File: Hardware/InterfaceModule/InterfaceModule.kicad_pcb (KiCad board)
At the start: 2 copper layers, 25 parts, among them J1 External MIC IN, J11 D-700 GPS, J12 D-700 COM, J13 D-700 MIC, J2 External COM, J3 GPS IN, J4 External GPS IN, J5 TS-480 MIC, J7 TS-480 COM, J8 TS-480 EXT.SP, J9 D-700 EXT.SP 1, K1 4PDT Relay, K10 3PDT Relay, K11 3PDT Relay, K12 3PDT Relay, K13 3PDT Relay, K14 3PDT Relay, K2 4PDT Relay, K3 4PDT Relay, K4 4PDT Relay, K5 3PDT Relay, K6 3PDT Relay, K7 3PDT Relay, K8 3PDT Relay, K9 3PDT Relay

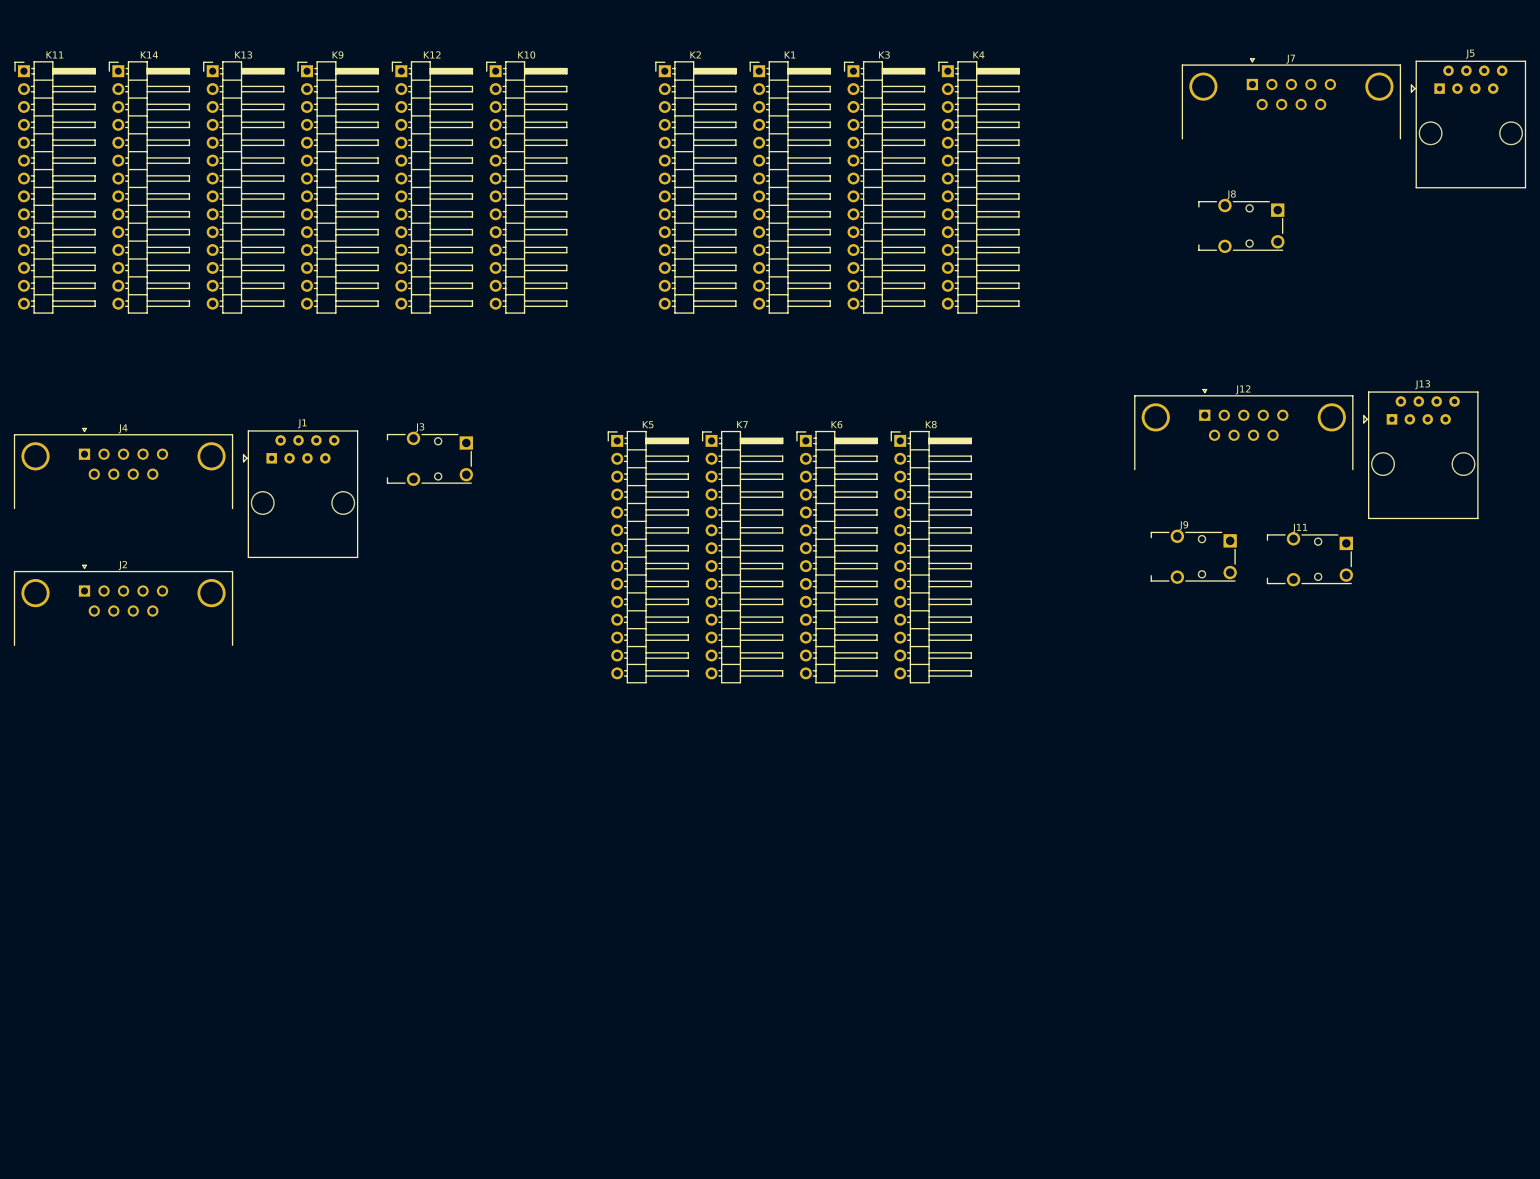
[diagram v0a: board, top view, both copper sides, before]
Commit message: Fixed labels
I don't know how to do busses properly, oh well
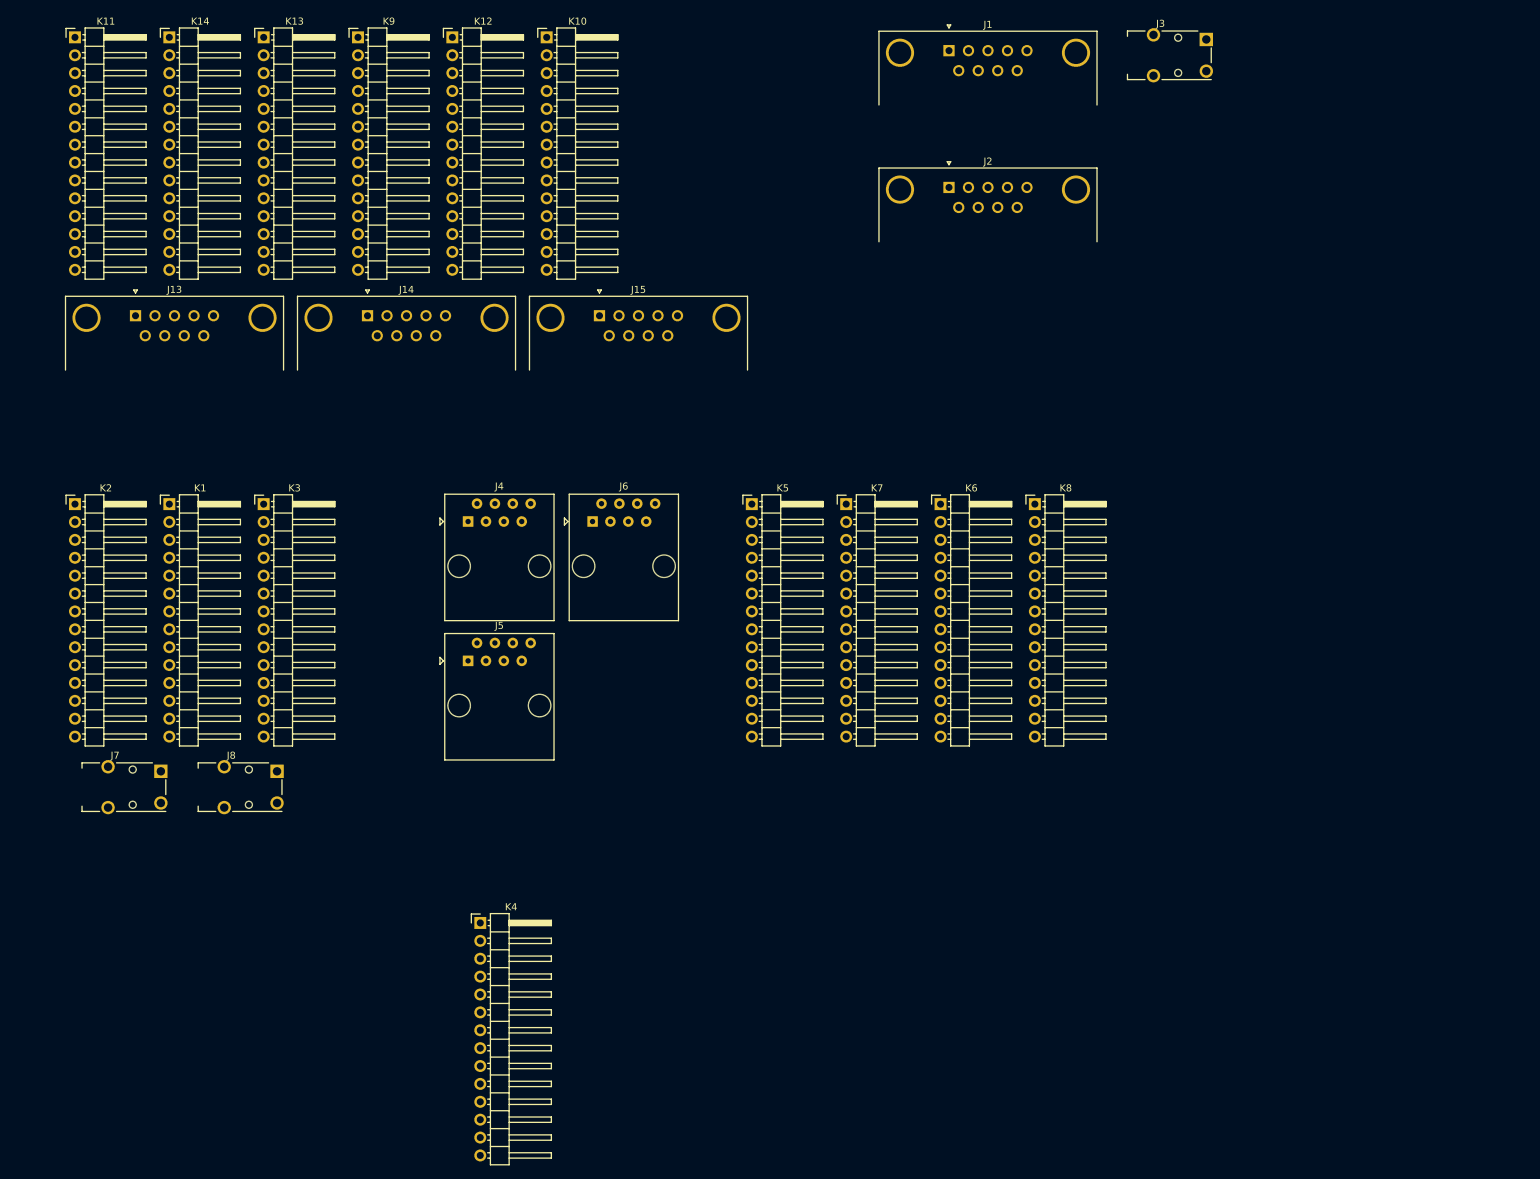
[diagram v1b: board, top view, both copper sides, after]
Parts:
- removed J11: D-700 GPS, Connector_Audio:Jack_3.5mm_Switronic_ST-005-G_horizontal
- removed J12: D-700 COM, Connector_Dsub:DSUB-9_Male_Horizontal_P2.77x2.84mm_EdgePinOffset4.94mm_Housed_MountingHolesOffset7.48mm
- removed J9: D-700 EXT.SP 1, Connector_Audio:Jack_3.5mm_Switronic_ST-005-G_horizontal
- added J14: TS-480 COM, Connector_Dsub:DSUB-9_Male_Horizontal_P2.77x2.84mm_EdgePinOffset4.94mm_Housed_MountingHolesOffset7.48mm, F.Cu at (100.4, 88.5)
- added J15: External COM, Connector_Dsub:DSUB-9_Male_Horizontal_P2.77x2.84mm_EdgePinOffset4.94mm_Housed_MountingHolesOffset7.48mm, F.Cu at (133.4, 88.5)
- added J6: TS-480 MIC, Connector_RJ:RJ45_Amphenol_54602-x08_Horizontal, F.Cu at (132.4, 117.8)
- J1: value External MIC IN -> External GPS IN; footprint Connector_RJ:RJ45_Amphenol_54602-x08_Horizontal -> Connector_Dsub:DSUB-9_Male_Horizontal_P2.77x2.84mm_EdgePinOffset4.94mm_Housed_MountingHolesOffset7.48mm
- J13: value D-700 MIC -> TS-480 COM; footprint Connector_RJ:RJ45_Amphenol_54602-x08_Horizontal -> Connector_Dsub:DSUB-9_Male_Horizontal_P2.77x2.84mm_EdgePinOffset4.94mm_Housed_MountingHolesOffset7.48mm
- J2: value External COM -> External GPS OUT
- J3: value GPS IN -> D-700 GPS
- J4: value External GPS IN -> External MIC IN; footprint Connector_Dsub:DSUB-9_Male_Horizontal_P2.77x2.84mm_EdgePinOffset4.94mm_Housed_MountingHolesOffset7.48mm -> Connector_RJ:RJ45_Amphenol_54602-x08_Horizontal
- J5: value TS-480 MIC -> D-700 MIC
- J7: value TS-480 COM -> D-700 EXT.SP 1; footprint Connector_Dsub:DSUB-9_Male_Horizontal_P2.77x2.84mm_EdgePinOffset4.94mm_Housed_MountingHolesOffset7.48mm -> Connector_Audio:Jack_3.5mm_Switronic_ST-005-G_horizontal
- moved J7 189.9 mm to (64.6, 155.5)
- moved J13 179.1 mm to (67.5, 88.5)
- moved J8 163.0 mm to (81.1, 155.5)
- moved J5 160.1 mm to (114.7, 137.6)
- moved K4 138.0 mm to (116.4, 174.8)
- moved J2 135.5 mm to (183.0, 70.3)
- moved J3 119.7 mm to (213.1, 51.6)
- moved J1 112.3 mm to (183.0, 50.9)
- moved K3 103.9 mm to (85.7, 115.3)
- moved K1 103.9 mm to (72.3, 115.3)
- moved K2 103.9 mm to (58.9, 115.3)
- moved J4 55.3 mm to (114.7, 117.8)
- moved K5 21.1 mm to (155.0, 115.3)
- moved K6 21.1 mm to (181.8, 115.3)
- moved K7 21.1 mm to (168.4, 115.3)
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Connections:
- net /Kenwood D-700 Connectors/D-700_DATA.DATA_DE renamed /Data Port Switching/DATA_DE
- net /Kenwood D-700 Connectors/D-700_DATA.DATA_PKD renamed /Data Port Switching/DATA_PKD
- net /Kenwood D-700 Connectors/D-700_DATA.DATA_PKS renamed /Data Port Switching/DATA_PKS
- net /Kenwood D-700 Connectors/D-700_DATA.DATA_PR1 renamed /Data Port Switching/DATA_PR1
- net /Kenwood D-700 Connectors/D-700_DATA.DATA_PR9 renamed /Data Port Switching/DATA_PR9
- net /Kenwood TS-480 Connectors/TS-480_DATA.DATA_ANG renamed /Data Port Switching/DATA_ANG
- net /Kenwood TS-480 Connectors/TS-480_DATA.DATA_ANI renamed /Data Port Switching/DATA_ANI
- net /Kenwood TS-480 Connectors/TS-480_DATA.DATA_ANO renamed /Data Port Switching/DATA_ANO
- net /Kenwood TS-480 Connectors/TS-480_DATA.DATA_DTS renamed /Data Port Switching/DATA_DTS
- net /Kenwood TS-480 Connectors/TS-480_DATA.DATA_NC renamed /Data Port Switching/DATA_NC
- J1 pad 1: /MIC_UP -> unconnected-(J1-Pad1)
- J1 pad 2: /MIC_8V -> Net-(J1-Pad2)
- J1 pad 3: /MIC_GND -> Net-(J1-Pad3)
- J1 pad 4: /MIC_PTT -> unconnected-(J1-Pad4)
- J1 pad 5: /MIC_MICGND -> GND
- J1 pad 6: /MIC_MIC -> unconnected-(J1-Pad6)
- J1 pad 7: /MIC_NC -> unconnected-(J1-Pad7)
- J1 pad 8: /MIC_DWN -> unconnected-(J1-Pad8)
- J13 pad 1: /Kenwood D-700 Connectors/MIC_UP -> /COM Port Switching/NC1
- J13 pad 2: /Kenwood D-700 Connectors/MIC_8V -> /COM Port Switching/RX
- J13 pad 3: /Kenwood D-700 Connectors/MIC_GND -> /COM Port Switching/TX
- J13 pad 4: /Kenwood D-700 Connectors/MIC_PTT -> /COM Port Switching/DTR
- J13 pad 5: /Kenwood D-700 Connectors/MIC_MICGND -> GND
- J13 pad 6: /Kenwood D-700 Connectors/MIC_MIC -> /COM Port Switching/DSR
- J13 pad 7: /Kenwood D-700 Connectors/MIC_NC -> /COM Port Switching/RTS
- J13 pad 8: /Kenwood D-700 Connectors/MIC_DWN -> /COM Port Switching/CTS
- J2 pad 1: /COM_NC1 -> unconnected-(J2-Pad1)
- J2 pad 2: /COM_RX -> Net-(J1-Pad2)
- J2 pad 3: /COM_TX -> Net-(J1-Pad3)
- J2 pad 4: /COM_DTR -> unconnected-(J2-Pad4)
- J2 pad 5: /COM_GND -> GND
- J2 pad 6: /COM_DSR -> unconnected-(J2-Pad6)
- J2 pad 7: /COM_RTS -> unconnected-(J2-Pad7)
- J2 pad 8: /COM_CTS -> unconnected-(J2-Pad8)
- J2 pad 9: /COM_NC2 -> unconnected-(J2-Pad9)
- J3 pad R: /EXTERNAL_GPS_IN.GPS_IN -> unconnected-(J3-PadR)
- J3 pad T: /EXTERNAL_GPS_IN.GPS_OUT -> Net-(J1-Pad2)
- J4 pad 1: unconnected-(J4-Pad1) -> /Microphone Switching/UP
- J4 pad 2: /EXTERNAL_GPS_IN.GPS_IN -> /Microphone Switching/8V
- J4 pad 3: /EXTERNAL_GPS_IN.GPS_OUT -> GND
- J4 pad 4: unconnected-(J4-Pad4) -> /Microphone Switching/PTT
- J4 pad 5: GND -> /Microphone Switching/MICGND
- J4 pad 6: unconnected-(J4-Pad6) -> /Microphone Switching/MIC
- J4 pad 7: unconnected-(J4-Pad7) -> /Microphone Switching/NC
- J4 pad 8: unconnected-(J4-Pad8) -> /Microphone Switching/DWN
- J5 pad 1: /Kenwood TS-480 Connectors/MIC_UP -> /Microphone Switching/UP
- J5 pad 2: /Kenwood TS-480 Connectors/MIC_8V -> /Microphone Switching/8V
- J5 pad 3: /Kenwood TS-480 Connectors/MIC_GND -> GND
- J5 pad 4: /Kenwood TS-480 Connectors/MIC_PTT -> /Microphone Switching/PTT
- J5 pad 5: /Kenwood TS-480 Connectors/MIC_MICGND -> /Microphone Switching/MICGND
- J5 pad 6: /Kenwood TS-480 Connectors/MIC_MIC -> /Microphone Switching/MIC
- J5 pad 7: /Kenwood TS-480 Connectors/MIC_NC -> /Microphone Switching/NC
- J5 pad 8: /Kenwood TS-480 Connectors/MIC_DWN -> /Microphone Switching/DWN
- J8 pad S: /Kenwood TS-480 Connectors/EXT.SP_S -> /Microphone Switching/SP_S
- J8 pad T: /Kenwood TS-480 Connectors/EXT.SP_T -> /Microphone Switching/SP_T
- K1 pad 11: /Kenwood D-700 Connectors/D-700_MIC.MIC_UP -> /Microphone Switching/UP
- K1 pad 12: /Kenwood D-700 Connectors/D-700_MIC.MIC_8V -> /Microphone Switching/8V
- K1 pad 13: /Kenwood D-700 Connectors/D-700_MIC.MIC_GND -> GND
- K1 pad 14: /Kenwood D-700 Connectors/D-700_MIC.MIC_PTT -> /Microphone Switching/PTT
- K1 pad 2: /Switching Network/Microphone Switching/MICROPHONE.MIC_UP -> /Microphone Switching/UP
- K1 pad 4: /Switching Network/Microphone Switching/MICROPHONE.MIC_8V -> /Microphone Switching/8V
- K1 pad 6: /Switching Network/Microphone Switching/MICROPHONE.MIC_GND -> GND
- K1 pad 8: /Switching Network/Microphone Switching/MICROPHONE.MIC_PTT -> /Microphone Switching/PTT
- K10 pad 2: /Kenwood D-700 Connectors/D-700_COM.COM_DTR -> /COM Port Switching/DTR
- K10 pad 3: /EXTERNAL_COM.COM_DSR -> /COM Port Switching/DSR
- K10 pad 4: /Kenwood D-700 Connectors/D-700_COM.COM_DSR -> /COM Port Switching/DSR
- K10 pad 5: /EXTERNAL_COM.COM_DTR -> /COM Port Switching/DTR
- K10 pad 6: /Kenwood D-700 Connectors/D-700_COM.COM_RX -> /COM Port Switching/RX
- K10 pad 7: /EXTERNAL_COM.COM_TX -> /COM Port Switching/TX
- K11 pad 2: /Kenwood TS-480 Connectors/TS-480_COM.COM_CTS -> /COM Port Switching/CTS
- K11 pad 3: /EXTERNAL_COM.COM_RTS -> /COM Port Switching/RTS
- K11 pad 4: /Kenwood TS-480 Connectors/TS-480_COM.COM_RX -> /COM Port Switching/RX
- K11 pad 5: /EXTERNAL_COM.COM_TX -> /COM Port Switching/TX
- K11 pad 6: /Kenwood TS-480 Connectors/TS-480_COM.COM_RTS -> /COM Port Switching/RTS
- K11 pad 7: /EXTERNAL_COM.COM_CTS -> /COM Port Switching/CTS
- K12 pad 2: /Kenwood D-700 Connectors/D-700_COM.COM_RTS -> /COM Port Switching/RTS
- K12 pad 3: /EXTERNAL_COM.COM_CTS -> /COM Port Switching/CTS
- K12 pad 4: /Kenwood D-700 Connectors/D-700_COM.COM_TX -> /COM Port Switching/TX
- K12 pad 5: /EXTERNAL_COM.COM_RX -> /COM Port Switching/RX
- K12 pad 6: /Kenwood D-700 Connectors/D-700_COM.COM_CTS -> /COM Port Switching/CTS
- K12 pad 7: /EXTERNAL_COM.COM_RTS -> /COM Port Switching/RTS
- K13 pad 2: /Kenwood TS-480 Connectors/TS-480_COM.COM_NC1 -> /COM Port Switching/NC1
- K13 pad 3: /EXTERNAL_COM.COM_NC1 -> /COM Port Switching/NC1
- K13 pad 4: /Kenwood TS-480 Connectors/TS-480_COM.COM_NC2 -> /COM Port Switching/NC2
- K13 pad 5: /EXTERNAL_COM.COM_NC2 -> /COM Port Switching/NC2
- K13 pad 6: /Kenwood TS-480 Connectors/TS-480_COM.COM_GND -> GND
- K13 pad 7: /EXTERNAL_COM.COM_GND -> GND
- K14 pad 2: /Kenwood D-700 Connectors/D-700_COM.COM_NC1 -> /COM Port Switching/NC1
- K14 pad 3: /EXTERNAL_COM.COM_NC1 -> /COM Port Switching/NC1
- K14 pad 4: /Kenwood D-700 Connectors/D-700_COM.COM_NC2 -> /COM Port Switching/NC2
- K14 pad 5: /EXTERNAL_COM.COM_NC2 -> /COM Port Switching/NC2
- K14 pad 6: /Kenwood D-700 Connectors/D-700_COM.COM_GND -> GND
- K14 pad 7: /EXTERNAL_COM.COM_GND -> GND
- K2 pad 11: /Kenwood TS-480 Connectors/TS-480_MIC.MIC_PTT -> /Microphone Switching/PTT
- K2 pad 12: /Kenwood TS-480 Connectors/TS-480_MIC.MIC_GND -> GND
- K2 pad 13: /Kenwood TS-480 Connectors/TS-480_MIC.MIC_8V -> /Microphone Switching/8V
- K2 pad 14: /Kenwood TS-480 Connectors/TS-480_MIC.MIC_UP -> /Microphone Switching/UP
- K2 pad 3: /Switching Network/Microphone Switching/MICROPHONE.MIC_PTT -> /Microphone Switching/PTT
- K2 pad 5: /Switching Network/Microphone Switching/MICROPHONE.MIC_GND -> GND
- K2 pad 7: /Switching Network/Microphone Switching/MICROPHONE.MIC_8V -> /Microphone Switching/8V
- K2 pad 9: /Switching Network/Microphone Switching/MICROPHONE.MIC_UP -> /Microphone Switching/UP
- K3 pad 11: /Switching Network/Microphone Switching/D-700_MIC.MICGND -> /Microphone Switching/MICGND
- K3 pad 12: /Kenwood D-700 Connectors/D-700_MIC.MIC_MIC -> /Microphone Switching/MIC
- K3 pad 13: /Kenwood D-700 Connectors/D-700_MIC.MIC_NC -> /Microphone Switching/NC
- K3 pad 14: /Kenwood D-700 Connectors/D-700_MIC.MIC_DWN -> /Microphone Switching/DWN
- K3 pad 2: /Switching Network/Microphone Switching/MICROPHONE.MIC_MICGND -> /Microphone Switching/MICGND
- K3 pad 3: /Switching Network/Microphone Switching/D-700_EXTSP1.SP_T -> /Microphone Switching/SP_T
- K3 pad 4: /Switching Network/Microphone Switching/MICROPHONE.MIC_MIC -> /Microphone Switching/MIC
- K3 pad 6: /Switching Network/Microphone Switching/MICROPHONE.MIC_NC -> /Microphone Switching/NC
- K3 pad 8: /Switching Network/Microphone Switching/MICROPHONE.MIC_DWN -> /Microphone Switching/DWN
- K4 pad 11: /Kenwood TS-480 Connectors/TS-480_MIC.MIC_DWN -> /Microphone Switching/DWN
- K4 pad 12: /Kenwood TS-480 Connectors/TS-480_MIC.MIC_NC -> /Microphone Switching/NC
- K4 pad 13: /Kenwood TS-480 Connectors/TS-480_MIC.MIC_MIC -> /Microphone Switching/MIC
- K4 pad 14: /Switching Network/Microphone Switching/TS-480_MIC.MICGND -> /Microphone Switching/MICGND
- K4 pad 3: /Switching Network/Microphone Switching/MICROPHONE.MIC_DWN -> /Microphone Switching/DWN
- K4 pad 5: /Switching Network/Microphone Switching/MICROPHONE.MIC_NC -> /Microphone Switching/NC
- K4 pad 7: /Switching Network/Microphone Switching/MICROPHONE.MIC_MIC -> /Microphone Switching/MIC
- K4 pad 8: /Switching Network/Microphone Switching/D-700_EXTSP1.SP_T -> /Microphone Switching/SP_T
- K4 pad 9: /Switching Network/Microphone Switching/MICROPHONE.MIC_MICGND -> /Microphone Switching/MICGND
- K5 pad 3: /SignaLink #2 Connectors/SignaLink4 -> /Data Port Switching/RADIO_4
- K5 pad 5: /SignaLink #2 Connectors/SignaLink1 -> /Data Port Switching/RADIO_1
- K5 pad 7: /SignaLink #2 Connectors/SignaLink5 -> /Data Port Switching/RADIO_5
- K6 pad 3: /SignaLink #1 Connectors/SignaLink0 -> /Data Port Switching/RADIO_0
- K6 pad 5: /SignaLink #1 Connectors/SignaLink1 -> /Data Port Switching/RADIO_1
- K6 pad 6: /Kenwood D-700 Connectors/D-700_DATA.DATA_SQC -> /Data Port Switching/DATA_SQC
- K6 pad 7: /SignaLink #1 Connectors/SignaLink2 -> /Data Port Switching/RADIO_2
- K7 pad 3: /SignaLink #2 Connectors/SignaLink3 -> /Data Port Switching/RADIO_3
- K7 pad 5: /SignaLink #2 Connectors/SignaLink0 -> /Data Port Switching/RADIO_0
- K7 pad 6: /Kenwood TS-480 Connectors/TS-480_DATA.DATA_SQC -> /Data Port Switching/DATA_SQC
- K7 pad 7: /SignaLink #2 Connectors/SignaLink2 -> /Data Port Switching/RADIO_2
- K8 pad 3: /SignaLink #1 Connectors/SignaLink3 -> /Data Port Switching/RADIO_3
- K8 pad 5: /SignaLink #1 Connectors/SignaLink4 -> /Data Port Switching/RADIO_4
- K8 pad 7: /SignaLink #1 Connectors/SignaLink5 -> /Data Port Switching/RADIO_5
- K9 pad 2: /Kenwood TS-480 Connectors/TS-480_COM.COM_DSR -> /COM Port Switching/DSR
- K9 pad 3: /EXTERNAL_COM.COM_DTR -> /COM Port Switching/DTR
- K9 pad 4: /Kenwood TS-480 Connectors/TS-480_COM.COM_DTR -> /COM Port Switching/DTR
- K9 pad 5: /EXTERNAL_COM.COM_DSR -> /COM Port Switching/DSR
- K9 pad 6: /Kenwood TS-480 Connectors/TS-480_COM.COM_TX -> /COM Port Switching/TX
- K9 pad 7: /EXTERNAL_COM.COM_RX -> /COM Port Switching/RX
